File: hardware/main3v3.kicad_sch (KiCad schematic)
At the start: 7 parts, among them U601 MP2143DJ-LF-Z

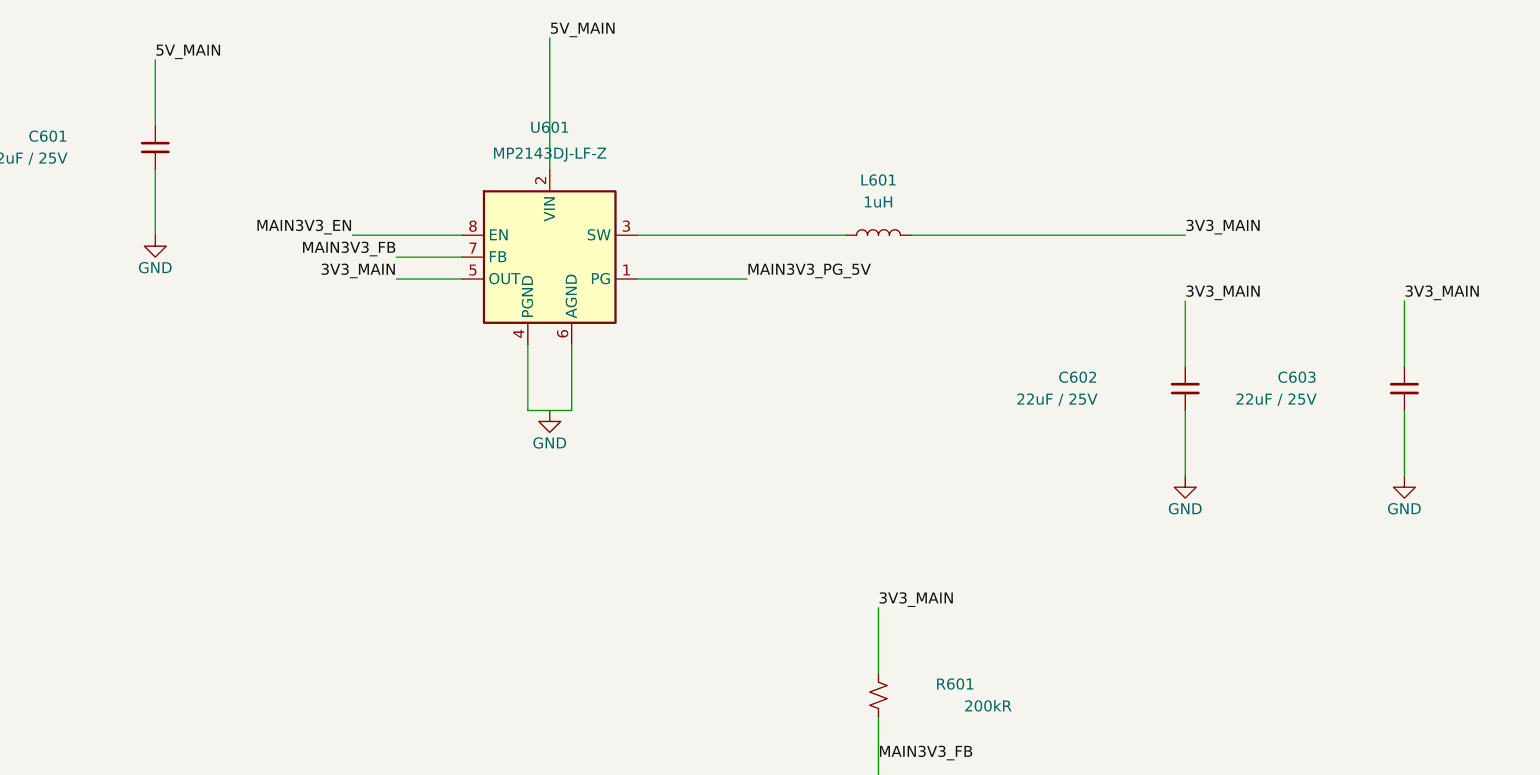
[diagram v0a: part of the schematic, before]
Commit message: Integrate main 3.3 V regulator and PMIC supply nets
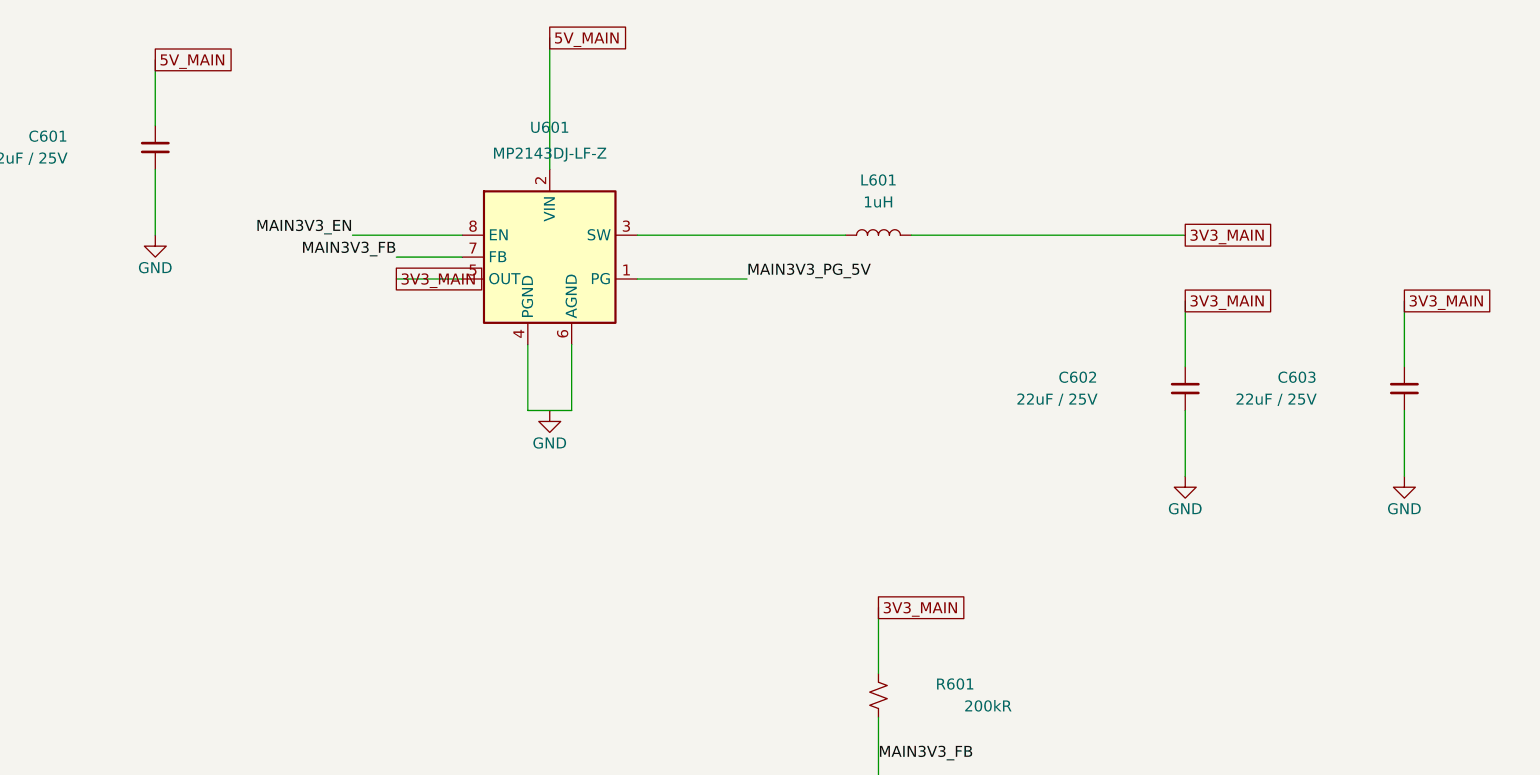
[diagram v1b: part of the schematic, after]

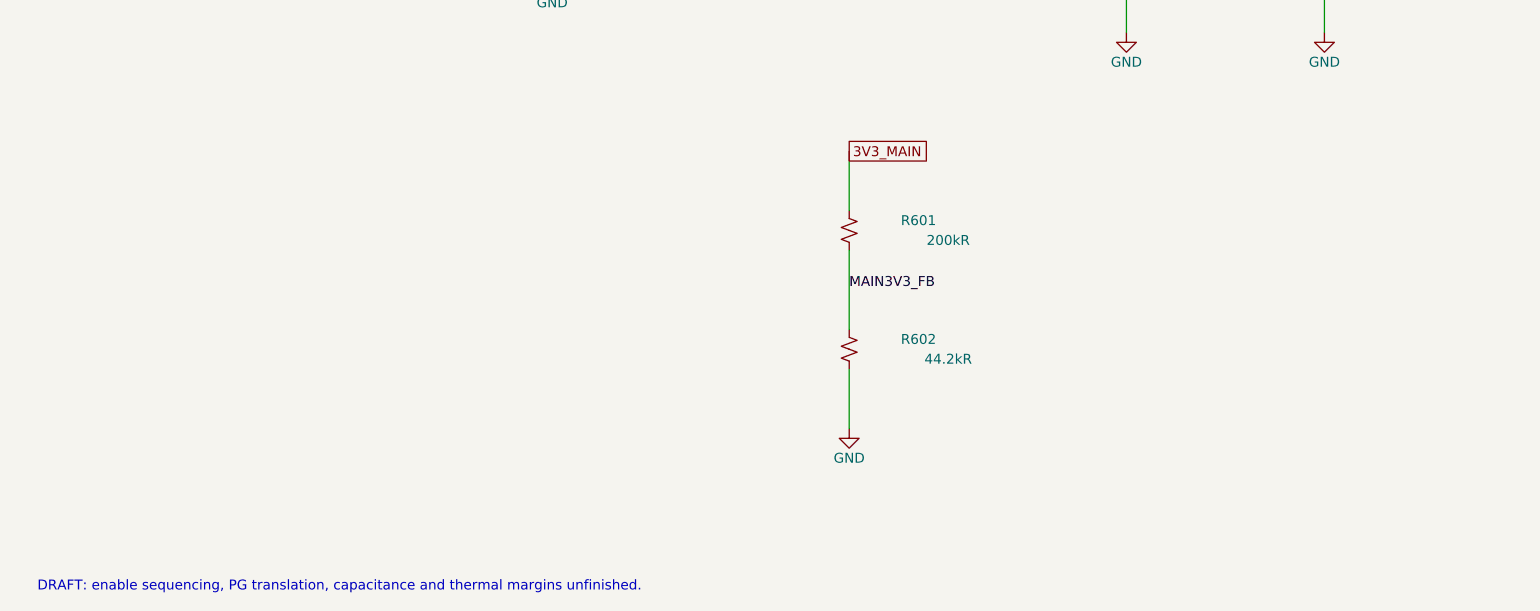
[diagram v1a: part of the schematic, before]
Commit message: Capture main 3.3 V enable divider from upstream 5 V
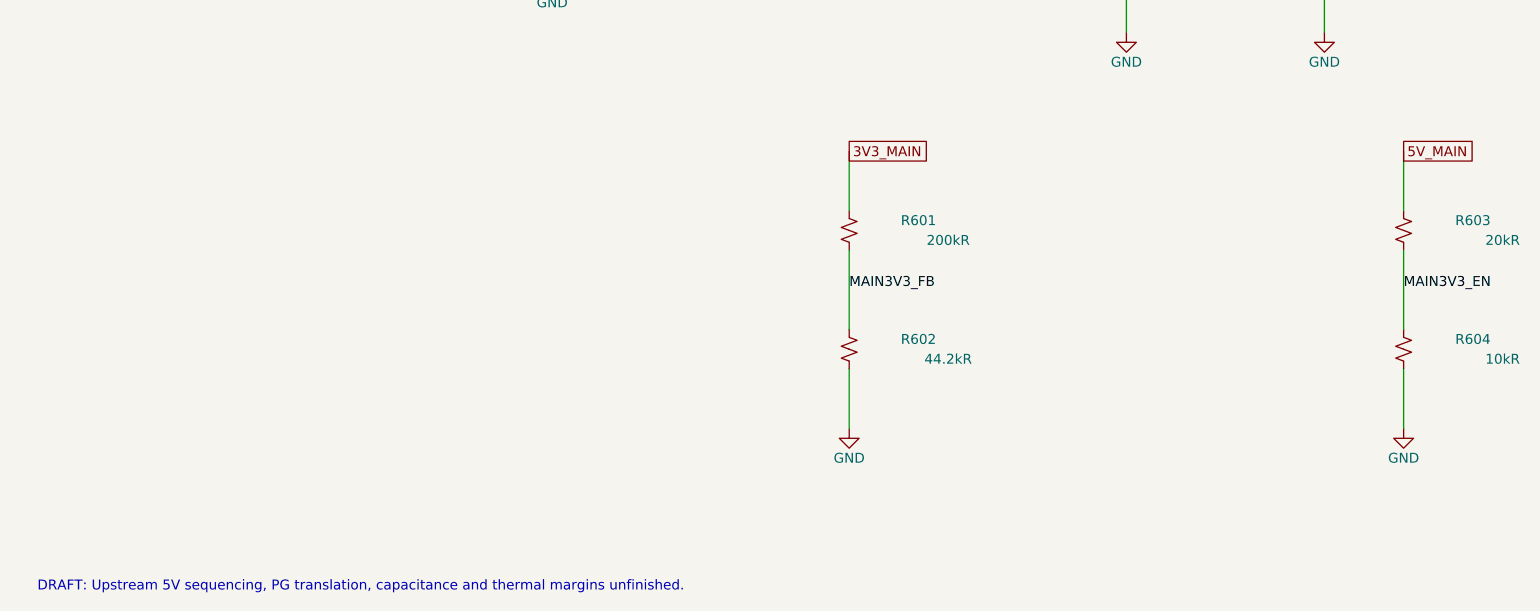
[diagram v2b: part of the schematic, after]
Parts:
- added R603: 20kR, Resistor_SMD:R_0603_1608Metric, symbol Device:R_Small_US
- added R604: 10kR, Resistor_SMD:R_0603_1608Metric, symbol Device:R_Small_US
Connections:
- net 5V_MAIN: now also R603.1
- net GND: now also R604.2
- net MAIN3V3_EN: now also R603.2, R604.1
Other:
- note added: "DRAFT: Upstream 5V sequencing, PG translation, capacitance and thermal margins unfinished."
- note removed: "DRAFT: enable sequencing, PG translation, capacitance and thermal margins unfinished."

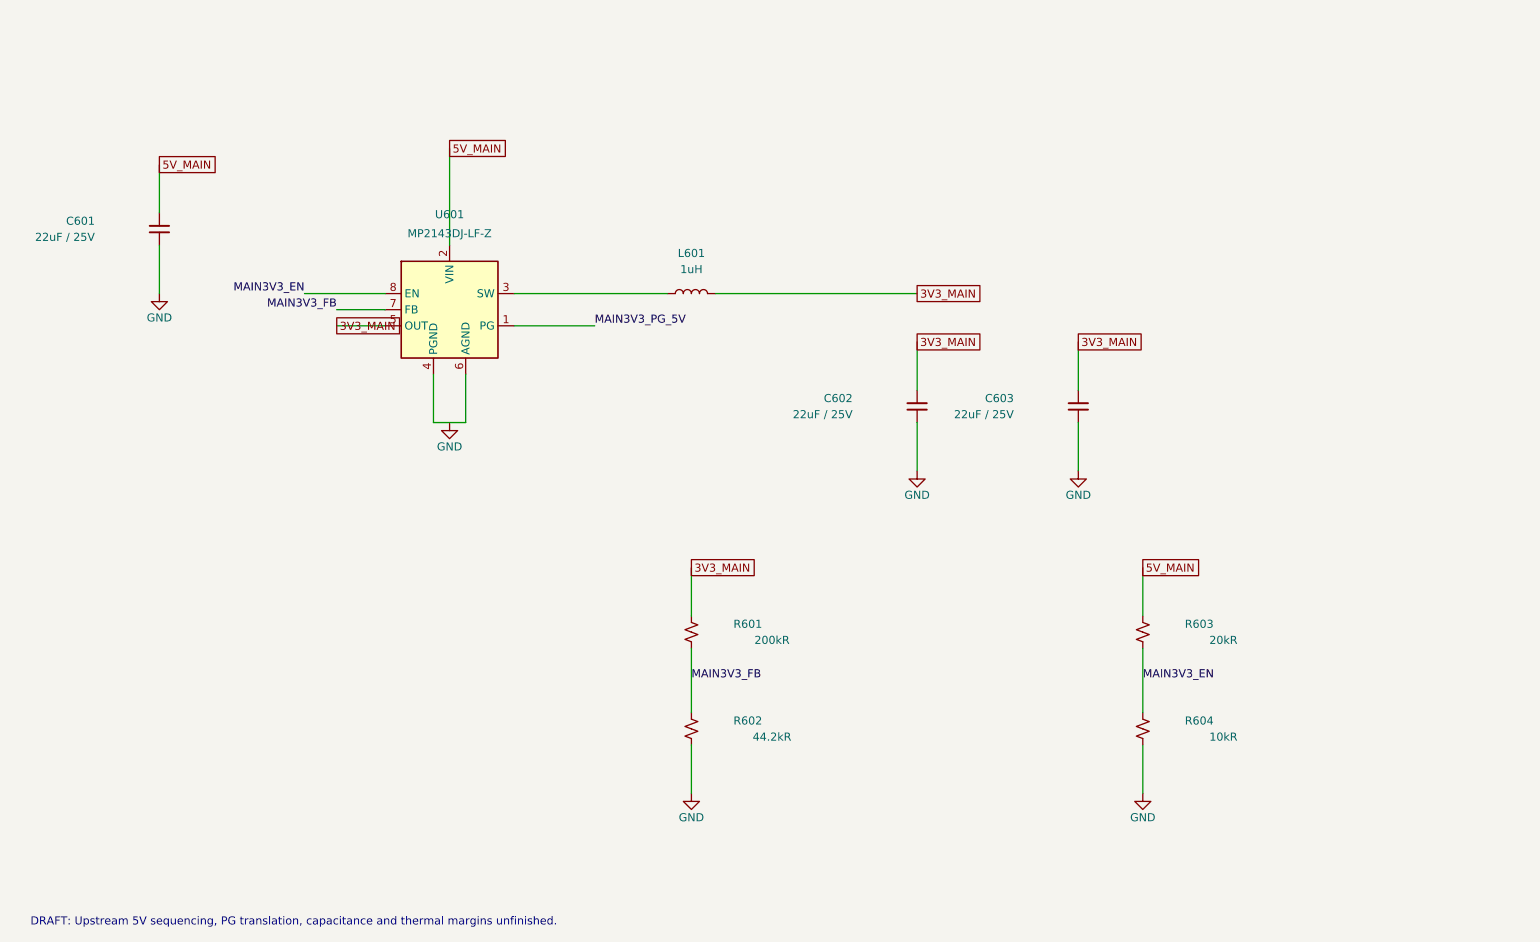
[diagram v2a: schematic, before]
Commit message: Capture main rail power-good buffer in recovery voltage domain
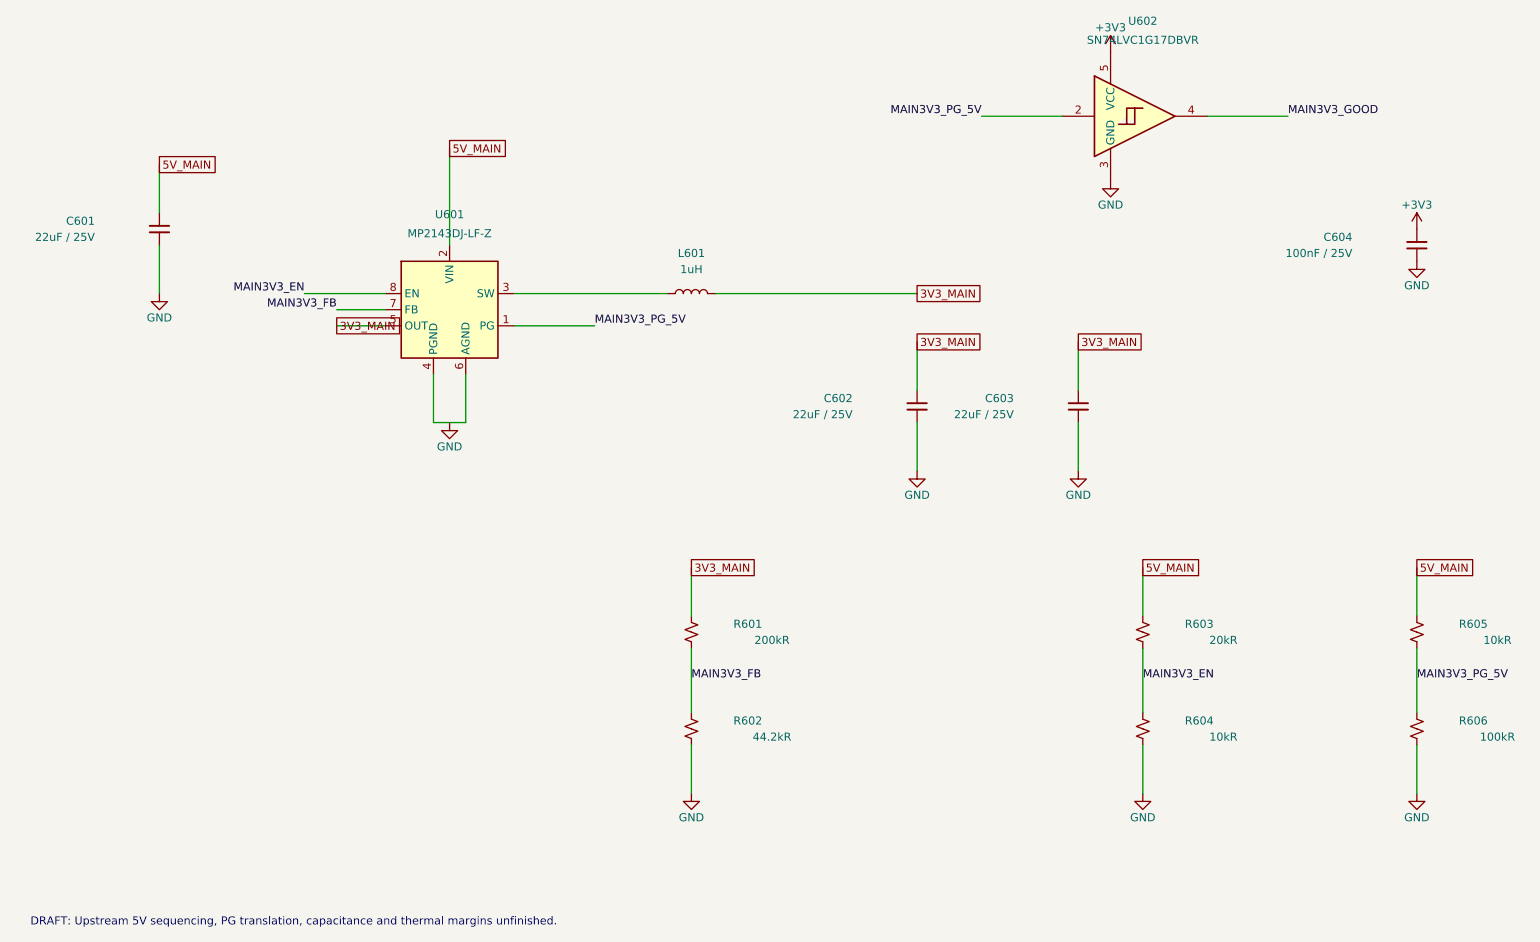
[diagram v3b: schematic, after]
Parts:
- added C604: 100nF / 25V, Capacitor_SMD:C_0603_1608Metric, symbol Device:C_Small
- added R605: 10kR, Resistor_SMD:R_0603_1608Metric, symbol Device:R_Small_US
- added R606: 100kR, Resistor_SMD:R_0603_1608Metric, symbol Device:R_Small_US
- added U602: SN74LVC1G17DBVR, Package_TO_SOT_SMD:SOT-23-5, symbol 74xGxx:74LVC1G17
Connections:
- net 5V_MAIN: now also R605.1
- net GND: now also C604.2, R606.2, U602.3 (GND)
- net MAIN3V3_PG_5V: now also R605.2, R606.1, U602.2
- new net +3V3: C604.1, U602.5 (VCC)
- new net MAIN3V3_GOOD: U602.4
